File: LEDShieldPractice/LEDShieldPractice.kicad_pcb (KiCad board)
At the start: 2 copper layers, 40 x 22.5 mm, 11 parts, among them J1 Conn_02x05_Odd_Even, J2 CLOCK_IN, Q1 2N3904

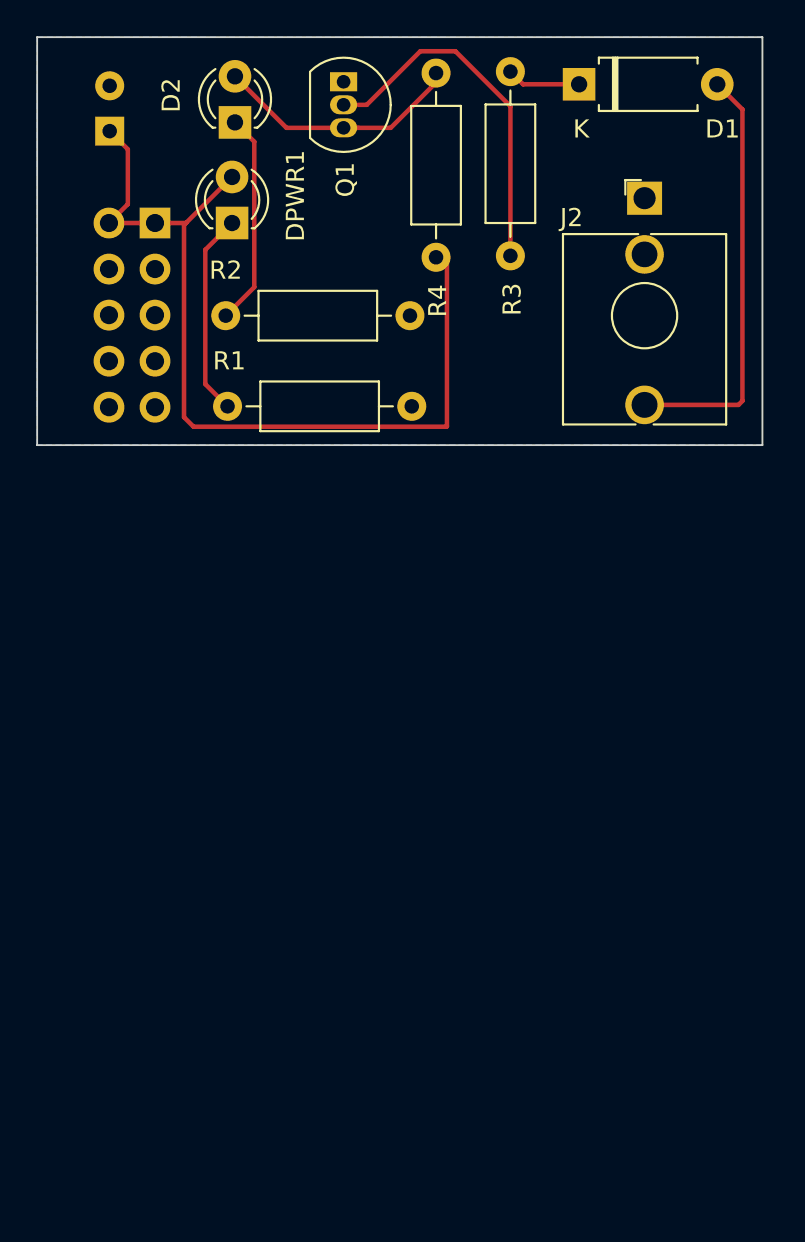
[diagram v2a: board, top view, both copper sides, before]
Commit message: Update LED Panel layout, added panel with mouse bites.
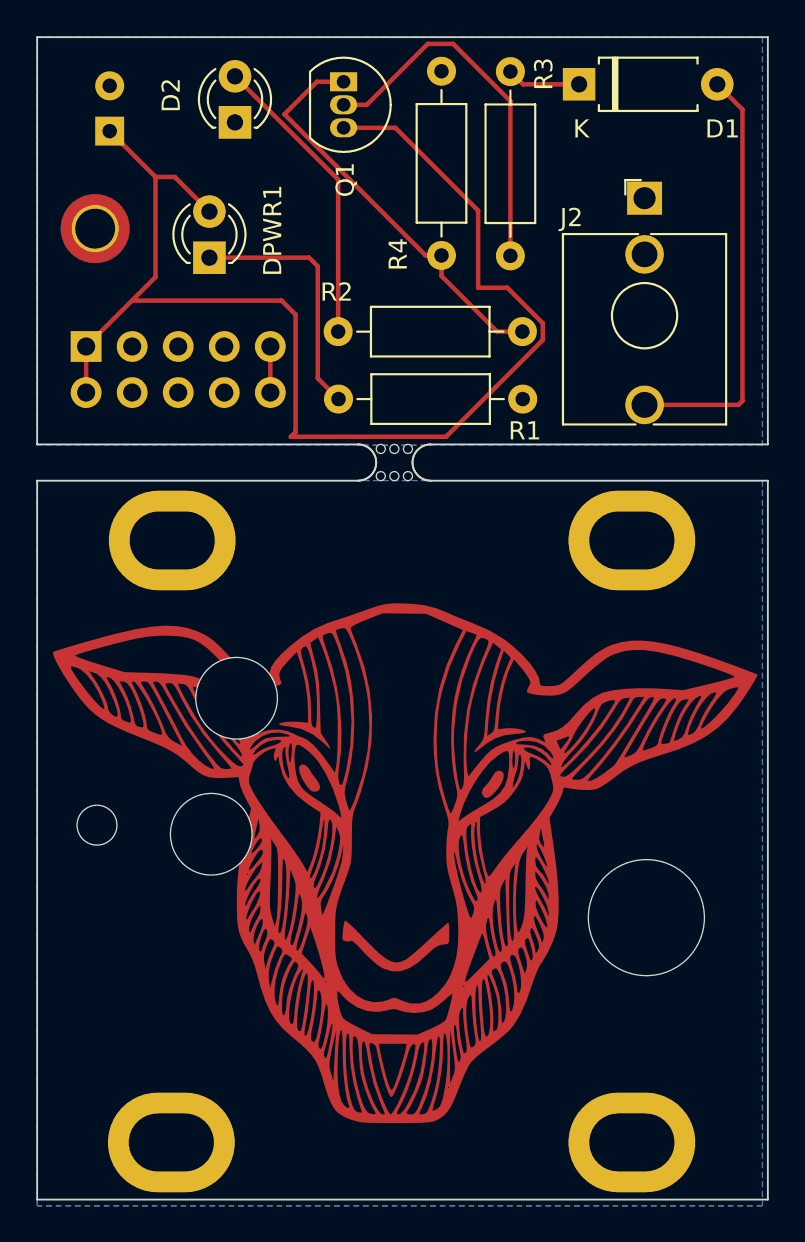
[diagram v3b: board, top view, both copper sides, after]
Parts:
- added G***: LOGO, ArtworkFootprints:SheepCopper, F.Cu at (44.9, 73.3)
- added G***: LOGO, ArtworkFootprints:SixteenWinds, B.Cu at (50.4, 35.8)
- added G***: LOGO, ArtworkFootprints:SheepSilk, B.Cu at (44.4, 71.5)
- added H1: MountingHole_Pad, MountingHole:MountingHole_3.2mm_M3_IntellijelOval_Pad, F.Cu at (57.3, 90.5)
- added H2: MountingHole_Pad, MountingHole:MountingHole_3.2mm_M3_IntellijelOval_Pad, F.Cu at (57.3, 57.3)
- added H3: MountingHole_Pad, MountingHole:MountingHole_3.2mm_M3_IntellijelOval_Pad, F.Cu at (31.9, 57.3)
- added H4: MountingHole_Pad, MountingHole:MountingHole_3.2mm_M3_IntellijelOval_Pad, F.Cu at (31.9, 90.5)
- added REF**: MountingHole_4.5mm, MountingHole:MountingHole_4.5mm, F.Cu at (34.1, 73.5)
- added REF**: MountingHole_6.4mm_M6, MountingHole:MountingHole_6.4mm_M6, F.Cu at (58.1, 78.1)
- added REF**: MountingHole_2.2mm_M2, MountingHole:MountingHole_2.2mm_M2, F.Cu at (27.8, 73.0)
- added REF**: MountingHole_4.5mm, MountingHole:MountingHole_4.5mm, F.Cu at (35.5, 66.0)
- added REF**: MountingHole_2.2mm_M2_DIN965_Pad_TopBottom, MountingHole:MountingHole_2.2mm_M2_DIN965_Pad_TopBottom, F.Cu at (27.7, 40.1)
- added mouse-bite-2mm-slot: VAL**, Panelization:mouse-bite-2mm-slot, F.Cu at (44.2, 53.0)
- moved R2 16.4 mm to (51.3, 45.7), turned to 180 degrees
- moved J1 7.80 mm to (27.2, 46.6), turned to -90 degrees
- moved R1 6.13 mm to (41.1, 49.5)
- moved DPWR1 2.28 mm to (34.0, 41.7)
- moved R4 0.32 mm to (46.8, 41.5)
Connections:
- D2 pad 1: Net-(D2-Pad1) -> GND
- D2 pad 2: CLOCK -> Net-(D2-Pad2)
- J1 pad 10: unconnected-(J1-Pad10) -> -12V
- J1 pad 9: unconnected-(J1-Pad9) -> -12V
- Q1 pad 1: GND -> CLOCK
- Q1 pad 3: CLOCK -> +12V
- R2 pad 1: Net-(D2-Pad1) -> CLOCK
- R2 pad 2: GND -> Net-(D2-Pad2)
- R4 pad 1: +12V -> CLOCK
- R4 pad 2: CLOCK -> GND
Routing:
- net +12V: track 48.6 -> 72.0 mm
- net Net-(D2-Pad2): track 0.00 -> 16.4 mm
- net Net-(D2-Pad1): track 11.8 -> 0.00 mm
- net CLOCK: track 14.2 -> 22.8 mm
- net Net-(DPWR1-Pad1): track 11.2 -> 14.0 mm
- net -12V: track 0.00 -> 2.54 mm
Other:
- board size 40 x 22.5 mm -> 40.3 x 64.1 mm
- board text added: "-12V Red Stripe"
- board text added: "BlinkPanelv2"
- board text removed: "-12V"
